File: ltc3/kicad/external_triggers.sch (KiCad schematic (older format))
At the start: 36 parts, among them IC5 TLP3542, IC6 TLP3542, IC7 TLP3542, IC8 TLP3542, M5 W28-XQ1A-0.25, M6 W28-XQ1A-0.25, M7 W28-XQ1A-0.25, M8 W28-XQ1A-0.25, P10 CONN_EXT_PWR_1, P11 CONN_EXT_PWR_3, P12 CONN_EXT_PWR_2, P13 CONN_EXT_PWR_4, P14 CONN_01X10, P15 CONN_01X08, P16 CONN_01X10, P17 CONN_01X08, Q4 PMV45EN, Q5 PMV45EN, Q6 PMV45EN, Q7 PMV45EN, SW10 SP3T, SW11 SP3T, SW8 SP3T, SW9 SP3T

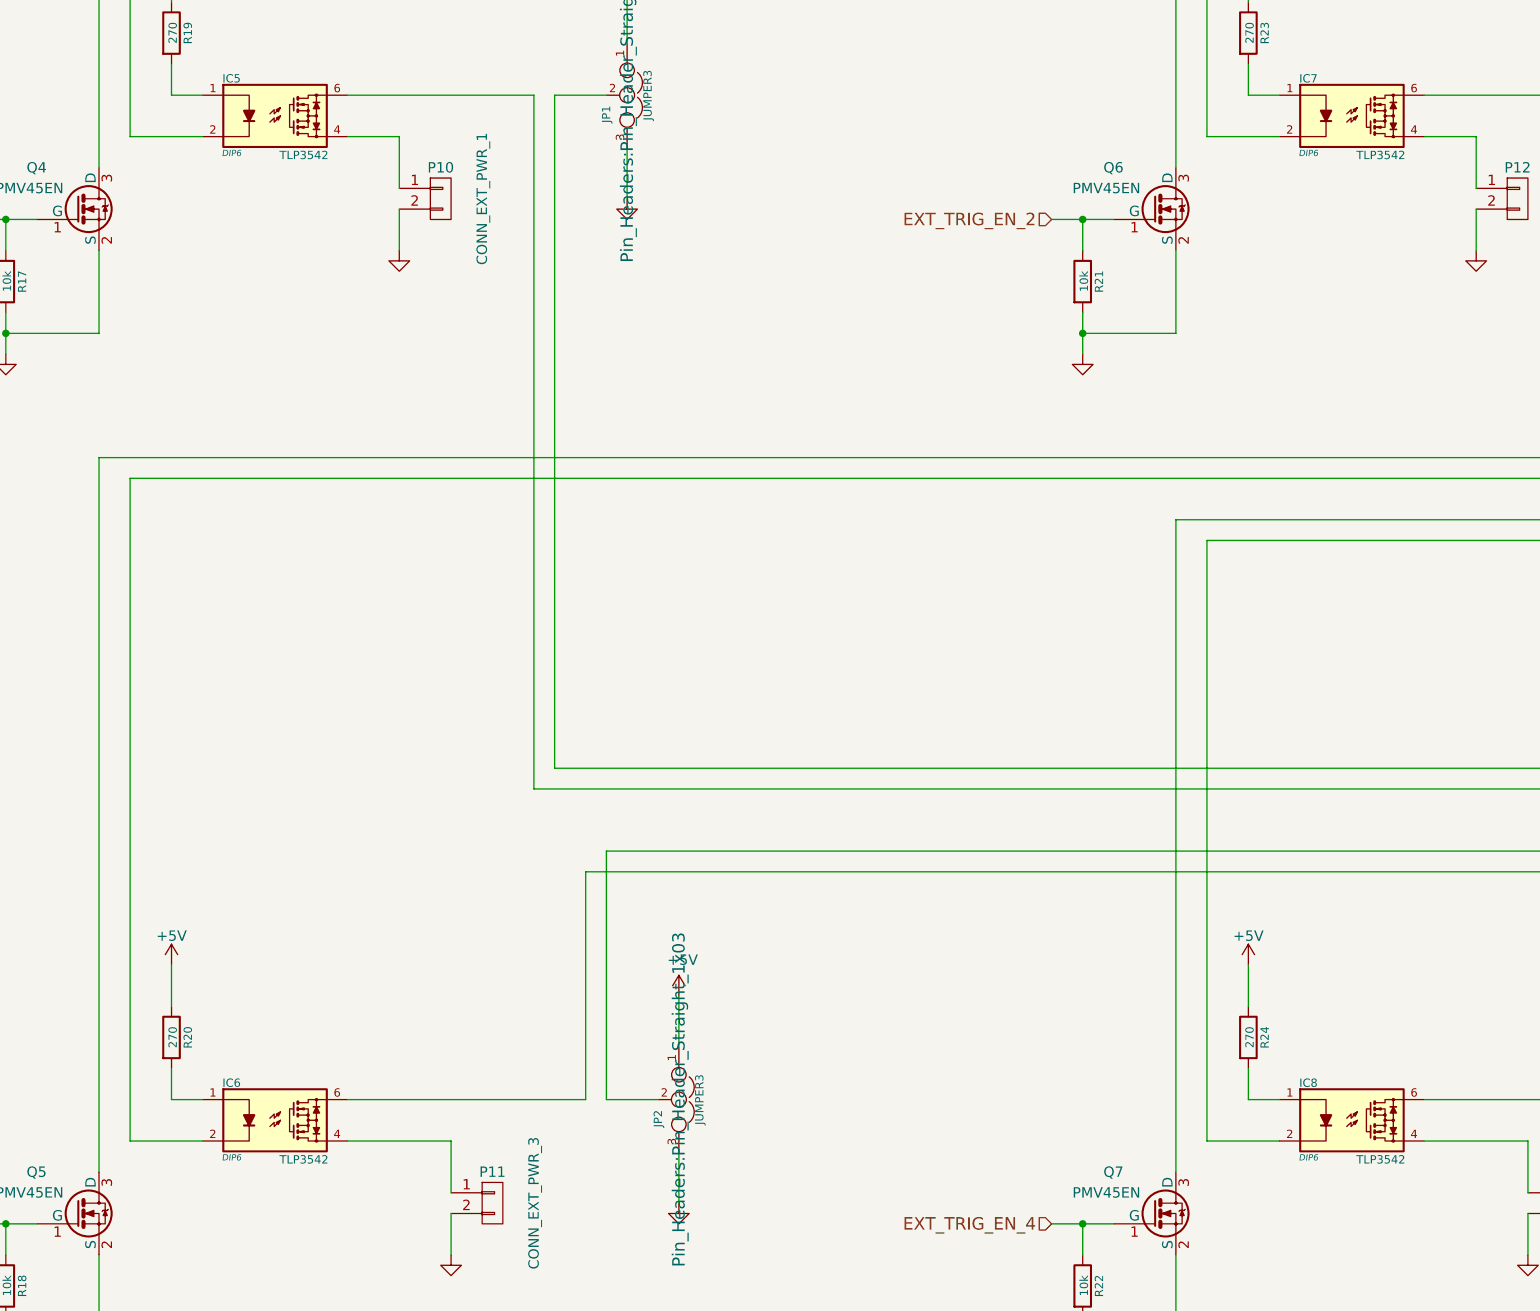
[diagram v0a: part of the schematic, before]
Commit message: Assigned more footprints, created PSOP-6 and PTN78020W.
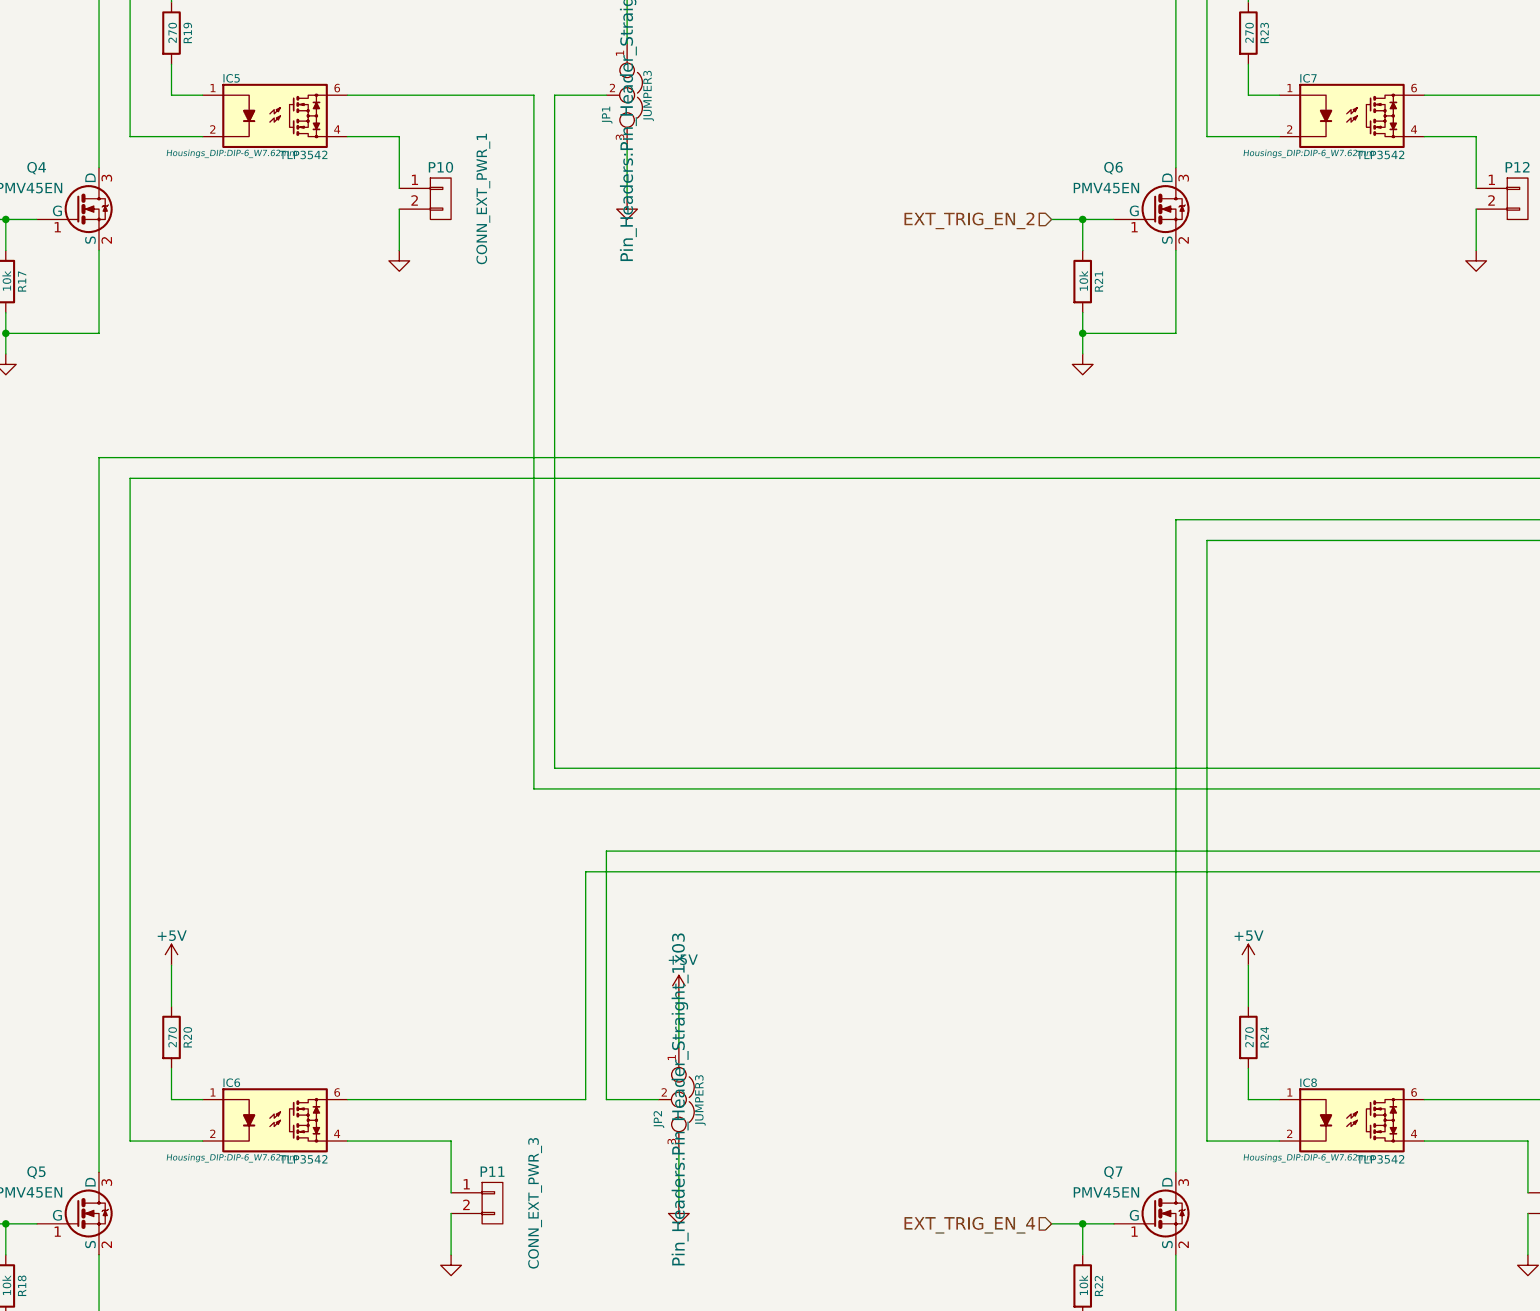
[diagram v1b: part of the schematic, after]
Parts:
- IC5, IC6, IC7, IC8: footprint DIP6 -> Housings_DIP:DIP-6_W7.62mm
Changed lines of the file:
@@
 LIBS:battery_single_cell
 LIBS:breakers
-LIBS:Launch_Tower_Computer_III-cache
 EELAYER 25 0
 EELAYER END
@@
 EXT_TRIG_EN_1
 $Comp
-L GND #PWR0168
+L GND #PWR0173
 U 1 1 56E098DE
 P 1650 4100
-F 0 "#PWR0168" H 1650 4100 30  0001 C CNN
+F 0 "#PWR0173" H 1650 4100 30  0001 C CNN
 F 1 "GND" H 1650 4030 30  0001 C CNN
 F 2 "" H 1650 4100 60  0000 C CNN
@@
 $EndComp
 $Comp
-L GND #PWR0169
+L GND #PWR0174
 U 1 1 56E098F2
 P 3550 3600
-F 0 "#PWR0169" H 3550 3600 30  0001 C CNN
+F 0 "#PWR0174" H 3550 3600 30  0001 C CNN
 F 1 "GND" H 3550 3530 30  0001 C CNN
 F 2 "" H 3550 3600 60  0000 C CNN
@@
 F 0 "IC5" H 2740 3230 40  0000 C CNN
 F 1 "TLP3542" H 3090 2860 40  0000 C CNN
-F 2 "DIP6" H 2740 2870 30  0000 C CIN
+F 2 "Housings_DIP:DIP-6_W7.62mm" H 2740 2870 30  0000 C CIN
 F 3 "" H 2950 3050 60  0000 C CNN
 	1    2950 3000
@@
 $EndComp
 $Comp
-L +5V #PWR0170
+L +5V #PWR0175
 U 1 1 56E09914
 P 2450 2200
-F 0 "#PWR0170" H 2450 2050 50  0001 C CNN
+F 0 "#PWR0175" H 2450 2050 50  0001 C CNN
 F 1 "+5V" H 2450 2340 50  0000 C CNN
 F 2 "" H 2450 2200 60  0000 C CNN
@@
 EXT_TRIG_EN_2
 $Comp
-L GND #PWR0171
+L GND #PWR0176
 U 1 1 56E09922
 P 6850 4100
-F 0 "#PWR0171" H 6850 4100 30  0001 C CNN
+F 0 "#PWR0176" H 6850 4100 30  0001 C CNN
 F 1 "GND" H 6850 4030 30  0001 C CNN
 F 2 "" H 6850 4100 60  0000 C CNN
@@
 $EndComp
 $Comp
-L GND #PWR0172
+L GND #PWR0177
 U 1 1 56E09936
 P 8750 3600
-F 0 "#PWR0172" H 8750 3600 30  0001 C CNN
+F 0 "#PWR0177" H 8750 3600 30  0001 C CNN
 F 1 "GND" H 8750 3530 30  0001 C CNN
 F 2 "" H 8750 3600 60  0000 C CNN
@@
 F 0 "IC7" H 7940 3230 40  0000 C CNN
 F 1 "TLP3542" H 8290 2860 40  0000 C CNN
-F 2 "DIP6" H 7940 2870 30  0000 C CIN
+F 2 "Housings_DIP:DIP-6_W7.62mm" H 7940 2870 30  0000 C CIN
 F 3 "" H 8150 3050 60  0000 C CNN
 	1    8150 3000
@@
 $EndComp
 $Comp
-L +5V #PWR0173
+L +5V #PWR0178
 U 1 1 56E09958
 P 7650 2200
-F 0 "#PWR0173" H 7650 2050 50  0001 C CNN
+F 0 "#PWR0178" H 7650 2050 50  0001 C CNN
 F 1 "+5V" H 7650 2340 50  0000 C CNN
 F 2 "" H 7650 2200 60  0000 C CNN
@@
 EXT_TRIG_EN_3
 $Comp
-L GND #PWR0174
+L GND #PWR0179
 U 1 1 56E0996C
 P 1650 8950
-F 0 "#PWR0174" H 1650 8950 30  0001 C CNN
+F 0 "#PWR0179" H 1650 8950 30  0001 C CNN
 F 1 "GND" H 1650 8880 30  0001 C CNN
 F 2 "" H 1650 8950 60  0000 C CNN
@@
 F 0 "IC6" H 2740 8080 40  0000 C CNN
 F 1 "TLP3542" H 3090 7710 40  0000 C CNN
-F 2 "DIP6" H 2740 7720 30  0000 C CIN
+F 2 "Housings_DIP:DIP-6_W7.62mm" H 2740 7720 30  0000 C CIN
 F 3 "" H 2950 7900 60  0000 C CNN
 	1    2950 7850
@@
 $EndComp
 $Comp
-L +5V #PWR0175
+L +5V #PWR0180
 U 1 1 56E0999C
 P 2450 7050
-F 0 "#PWR0175" H 2450 6900 50  0001 C CNN
+F 0 "#PWR0180" H 2450 6900 50  0001 C CNN
 F 1 "+5V" H 2450 7190 50  0000 C CNN
 F 2 "" H 2450 7050 60  0000 C CNN
@@
 EXT_TRIG_EN_4
 $Comp
-L GND #PWR0176
+L GND #PWR0181
 U 1 1 56E099AA
 P 6850 8950
-F 0 "#PWR0176" H 6850 8950 30  0001 C CNN
+F 0 "#PWR0181" H 6850 8950 30  0001 C CNN
 F 1 "GND" H 6850 8880 30  0001 C CNN
 F 2 "" H 6850 8950 60  0000 C CNN
@@
 $EndComp
 $Comp
-L GND #PWR0177
+L GND #PWR0182
 U 1 1 56E099BE
 P 9000 8450
-F 0 "#PWR0177" H 9000 8450 30  0001 C CNN
+F 0 "#PWR0182" H 9000 8450 30  0001 C CNN
 F 1 "GND" H 9000 8380 30  0001 C CNN
 F 2 "" H 9000 8450 60  0000 C CNN
@@
 F 0 "IC8" H 7940 8080 40  0000 C CNN
 F 1 "TLP3542" H 8290 7710 40  0000 C CNN
-F 2 "DIP6" H 7940 7720 30  0000 C CIN
+F 2 "Housings_DIP:DIP-6_W7.62mm" H 7940 7720 30  0000 C CIN
 F 3 "" H 8150 7900 60  0000 C CNN
 	1    8150 7850
@@
 $EndComp
 $Comp
-L +5V #PWR0178
+L +5V #PWR0183
 U 1 1 56E099E0
 P 7650 7050
-F 0 "#PWR0178" H 7650 6900 50  0001 C CNN
+F 0 "#PWR0183" H 7650 6900 50  0001 C CNN
 F 1 "+5V" H 7650 7190 50  0000 C CNN
 F 2 "" H 7650 7050 60  0000 C CNN
@@
 Manual Override Switches, Front Panel
 $Comp
-L GND #PWR0179
+L GND #PWR0184
 U 1 1 56E09A12
 P 11800 2800
-F 0 "#PWR0179" H 11800 2550 50  0001 C CNN
+F 0 "#PWR0184" H 11800 2550 50  0001 C CNN
 F 1 "GND" H 11808 2626 50  0001 C CNN
 F 2 "" H 11800 2800 50  0000 C CNN
@@
 $EndComp
 $Comp
-L GND #PWR0180
+L GND #PWR0185
 U 1 1 56E38916
 P 3800 8450
-F 0 "#PWR0180" H 3800 8200 50  0001 C CNN
+F 0 "#PWR0185" H 3800 8200 50  0001 C CNN
 F 1 "GND" H 3808 8276 50  0001 C CNN
 F 2 "" H 3800 8450 50  0000 C CNN
@@
 $EndComp
 $Comp
-L GND #PWR0181
+L GND #PWR0186
 U 1 1 56E4925E
 P 4650 3350
-F 0 "#PWR0181" H 4650 3350 30  0001 C CNN
+F 0 "#PWR0186" H 4650 3350 30  0001 C CNN
 F 1 "GND" H 4650 3280 30  0001 C CNN
 F 2 "" H 4650 3350 60  0000 C CNN
@@
 $EndComp
 $Comp
-L GND #PWR0182
+L GND #PWR0187
 U 1 1 56E59F41
 P 9850 3350
-F 0 "#PWR0182" H 9850 3350 30  0001 C CNN
+F 0 "#PWR0187" H 9850 3350 30  0001 C CNN
 F 1 "GND" H 9850 3280 30  0001 C CNN
 F 2 "" H 9850 3350 60  0000 C CNN
@@
 $EndComp
 $Comp
-L GND #PWR0183
+L GND #PWR0188
 U 1 1 56E5B108
 P 4900 8200
-F 0 "#PWR0183" H 4900 8200 30  0001 C CNN
+F 0 "#PWR0188" H 4900 8200 30  0001 C CNN
 F 1 "GND" H 4900 8130 30  0001 C CNN
 F 2 "" H 4900 8200 60  0000 C CNN
@@
 $EndComp
 $Comp
-L GND #PWR0184
+L GND #PWR0189
 U 1 1 56E5BBF0
 P 10100 8200
-F 0 "#PWR0184" H 10100 8200 30  0001 C CNN
+F 0 "#PWR0189" H 10100 8200 30  0001 C CNN
 F 1 "GND" H 10100 8130 30  0001 C CNN
 F 2 "" H 10100 8200 60  0000 C CNN
@@
 	10100 8200 10100 7950
 $Comp
-L +5V #PWR0185
+L +5V #PWR0190
 U 1 1 56E5FD25
 P 9850 2350
-F 0 "#PWR0185" H 9850 2200 50  0001 C CNN
+F 0 "#PWR0190" H 9850 2200 50  0001 C CNN
 F 1 "+5V" H 9868 2524 50  0000 C CNN
 F 2 "" H 9850 2350 50  0000 C CNN
@@
 	9400 6400 12050 6400
 $Comp
-L +5V #PWR0186
+L +5V #PWR0191
 U 1 1 56E716C4
 P 4650 2350
-F 0 "#PWR0186" H 4650 2200 50  0001 C CNN
+F 0 "#PWR0191" H 4650 2200 50  0001 C CNN
 F 1 "+5V" H 4668 2524 50  0000 C CNN
 F 2 "" H 4650 2350 50  0000 C CNN
@@
 $EndComp
 $Comp
-L +5V #PWR0187
+L +5V #PWR0192
 U 1 1 56E72140
 P 4900 7200
-F 0 "#PWR0187" H 4900 7050 50  0001 C CNN
+F 0 "#PWR0192" H 4900 7050 50  0001 C CNN
 F 1 "+5V" H 4918 7374 50  0000 C CNN
 F 2 "" H 4900 7200 50  0000 C CNN
@@
 	4900 7200 4900 7450
 $Comp
-L +5V #PWR0188
+L +5V #PWR0193
 U 1 1 56E727AE
 P 10100 7200
-F 0 "#PWR0188" H 10100 7050 50  0001 C CNN
+F 0 "#PWR0193" H 10100 7050 50  0001 C CNN
 F 1 "+5V" H 10118 7374 50  0000 C CNN
 F 2 "" H 10100 7200 50  0000 C CNN

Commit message: LTC3: Cosmetic changes; reference designator updates; etc.
1. Renamed "PHNTM*" reference designators to something more
   conventional and descriptive (e.g., "PHNTM*" to "BT*" for off-board
   batteries).
2. Cosmetic changes to battery management and BeagleBone schematics
   (normalizing text notes style, etc.).
3. Incremental progress on footprint assignment.
4. Imported netlist into PCB layout editor, just for grins.
   Everything fits into a 250x135mm board.  Only $260 for an OSH Park run!
   There may be some opportunities for improvement...
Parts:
- M5, M6, M7, M8, SW10, SW11, SW8, SW9: footprint (none) -> Oddities:Dummy_Empty
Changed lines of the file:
@@
 F 0 "M5" H 13950 7225 50  0000 C CNN
 F 1 "W28-XQ1A-0.25" H 13950 7025 50  0000 C CNN
-F 2 "" H 13950 7100 50  0001 C CNN
+F 2 "Oddities:Dummy_Empty" H 13950 7100 50  0001 C CNN
 F 3 "" H 13950 7100 50  0000 C CNN
 	1    13950 7100
@@
 F 0 "SW8" V 13704 2648 50  0000 R CNN
 F 1 "SP3T" V 13796 2648 50  0000 R CNN
-F 2 "" H 13125 2975 50  0001 C CNN
+F 2 "Oddities:Dummy_Empty" H 13125 2975 50  0001 C CNN
 F 3 "" H 13125 2975 50  0000 C CNN
 	1    13750 2800
@@
 F 0 "SW9" V 14446 2648 50  0000 R CNN
 F 1 "SP3T" V 14354 2648 50  0000 R CNN
-F 2 "" H 13775 2975 50  0001 C CNN
+F 2 "Oddities:Dummy_Empty" H 13775 2975 50  0001 C CNN
 F 3 "" H 13775 2975 50  0000 C CNN
 	1    14400 2800
@@
 F 0 "SW10" V 15096 2648 50  0000 R CNN
 F 1 "SP3T" V 15004 2648 50  0000 R CNN
-F 2 "" H 14425 2975 50  0001 C CNN
+F 2 "Oddities:Dummy_Empty" H 14425 2975 50  0001 C CNN
 F 3 "" H 14425 2975 50  0000 C CNN
 	1    15050 2800
@@
 F 0 "SW11" V 15746 2648 50  0000 R CNN
 F 1 "SP3T" V 15654 2648 50  0000 R CNN
-F 2 "" H 15075 2975 50  0001 C CNN
+F 2 "Oddities:Dummy_Empty" H 15075 2975 50  0001 C CNN
 F 3 "" H 15075 2975 50  0000 C CNN
 	1    15700 2800
@@
 F 0 "M6" H 14350 7225 50  0000 C CNN
 F 1 "W28-XQ1A-0.25" H 14350 7025 50  0000 C CNN
-F 2 "" H 14350 7100 50  0001 C CNN
+F 2 "Oddities:Dummy_Empty" H 14350 7100 50  0001 C CNN
 F 3 "" H 14350 7100 50  0000 C CNN
 	1    14350 7100
@@
 F 0 "M7" H 14750 7225 50  0000 C CNN
 F 1 "W28-XQ1A-0.25" H 14750 7025 50  0000 C CNN
-F 2 "" H 14750 7100 50  0001 C CNN
+F 2 "Oddities:Dummy_Empty" H 14750 7100 50  0001 C CNN
 F 3 "" H 14750 7100 50  0000 C CNN
 	1    14750 7100
@@
 F 0 "M8" H 15150 7225 50  0000 C CNN
 F 1 "W28-XQ1A-0.25" H 15150 7025 50  0000 C CNN
-F 2 "" H 15150 7100 50  0001 C CNN
+F 2 "Oddities:Dummy_Empty" H 15150 7100 50  0001 C CNN
 F 3 "" H 15150 7100 50  0000 C CNN
 	1    15150 7100

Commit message: Minor adjustment to BB cape footprint; more footprint assignments.
NB: "Valve" footprints are placeholder for components not yet
assigned.
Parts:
- P10, P11, P12, P13: footprint Pin_Headers:Pin_Header_Straight_1x02 -> Valves:VALVE-OCTAL
- P14, P16: footprint Pin_Headers:Pin_Header_Straight_1x10 -> Valves:VALVE-OCTAL
- P15, P17: footprint Pin_Headers:Pin_Header_Straight_1x08 -> Valves:VALVE-OCTAL
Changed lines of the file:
@@
 F 0 "P10" H 3750 3500 50  0000 C CNN
 F 1 "CONN_EXT_PWR_1" V 3950 3350 50  0000 C CNN
-F 2 "Pin_Headers:Pin_Header_Straight_1x02" H 3750 3350 60  0001 C CNN
+F 2 "Valves:VALVE-OCTAL" H 3750 3350 60  0001 C CNN
 F 3 "" H 3750 3350 60  0000 C CNN
 	1    3750 3350
@@
 F 0 "P12" H 8950 3500 50  0000 C CNN
 F 1 "CONN_EXT_PWR_2" V 9150 3350 50  0000 C CNN
-F 2 "Pin_Headers:Pin_Header_Straight_1x02" H 8950 3350 60  0001 C CNN
+F 2 "Valves:VALVE-OCTAL" H 8950 3350 60  0001 C CNN
 F 3 "" H 8950 3350 60  0000 C CNN
 	1    8950 3350
@@
 F 0 "P11" H 4000 8350 50  0000 C CNN
 F 1 "CONN_EXT_PWR_3" V 4200 8200 50  0000 C CNN
-F 2 "Pin_Headers:Pin_Header_Straight_1x02" H 4000 8200 60  0001 C CNN
+F 2 "Valves:VALVE-OCTAL" H 4000 8200 60  0001 C CNN
 F 3 "" H 4000 8200 60  0000 C CNN
 	1    4000 8200
@@
 F 0 "P13" H 9200 8350 50  0000 C CNN
 F 1 "CONN_EXT_PWR_4" V 9400 8200 50  0000 C CNN
-F 2 "Pin_Headers:Pin_Header_Straight_1x02" H 9200 8200 60  0001 C CNN
+F 2 "Valves:VALVE-OCTAL" H 9200 8200 60  0001 C CNN
 F 3 "" H 9200 8200 60  0000 C CNN
 	1    9200 8200
@@
 F 0 "P15" H 12250 6950 50  0000 L CNN
 F 1 "CONN_01X08" V 12400 6250 50  0000 L CNN
-F 2 "Pin_Headers:Pin_Header_Straight_1x08" H 12250 6450 50  0001 C CNN
+F 2 "Valves:VALVE-OCTAL" H 12250 6450 50  0001 C CNN
 F 3 "" H 12250 6450 50  0000 C CNN
 	1    12250 6450
@@
 F 0 "P17" H 13000 6950 50  0000 L CNN
 F 1 "CONN_01X08" V 13150 6250 50  0000 L CNN
-F 2 "Pin_Headers:Pin_Header_Straight_1x08" H 13000 6450 50  0001 C CNN
+F 2 "Valves:VALVE-OCTAL" H 13000 6450 50  0001 C CNN
 F 3 "" H 13000 6450 50  0000 C CNN
 	1    13000 6450
@@
 F 0 "P14" H 12250 2650 50  0000 L CNN
 F 1 "CONN_01X10" V 12400 1600 50  0000 L CNN
-F 2 "Pin_Headers:Pin_Header_Straight_1x10" H 12250 2100 50  0001 C CNN
+F 2 "Valves:VALVE-OCTAL" H 12250 2100 50  0001 C CNN
 F 3 "" H 12250 2100 50  0000 C CNN
 	1    12250 2100
@@
 F 0 "P16" H 13000 2650 50  0000 L CNN
 F 1 "CONN_01X10" V 13150 1600 50  0000 L CNN
-F 2 "Pin_Headers:Pin_Header_Straight_1x10" H 13000 2100 50  0001 C CNN
+F 2 "Valves:VALVE-OCTAL" H 13000 2100 50  0001 C CNN
 F 3 "" H 13000 2100 50  0000 C CNN
 	1    13000 2100

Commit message: LTC3: Progress on component value validation, footprint assignment.
1. Added datasheets for large-valued capacitors (Panasonic),
   high-current connectors (Molex MicroFit), etc.
2. Added footprint for BeagleBone Black cape connector.
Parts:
- JP801: renamed from JP1; value JUMPER3 -> Trigger Level
- JP802: renamed from JP3; value JUMPER3 -> Trigger Level
- JP803: renamed from JP2; value JUMPER3 -> Trigger Level
- JP804: renamed from JP4; value JUMPER3 -> Trigger Level
- renumbered IC5 to IC801, IC7 to IC802, IC6 to IC803, IC8 to IC804, M5 to M801, M6 to M802, M7 to M803, M8 to M804, P14 to P801, P16 to P802, P10 to P803, P12 to P804, P15 to P805, P17 to P806, P11 to P807, P13 to P808, Q4 to Q801, Q6 to Q802, Q5 to Q803, Q7 to Q804, R19 to R801, R23 to R802, R17 to R803, R21 to R804, R20 to R805, R24 to R806, R18 to R807, R22 to R808, SW8 to SW801, SW9 to SW802, SW10 to SW803, SW11 to SW804
